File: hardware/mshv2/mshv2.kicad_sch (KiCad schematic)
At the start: 0 parts

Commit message: Finished part 1
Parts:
- added C1: 100uF/25V, symbol Device:C_Polarized
- added C2: 100uF/10V, symbol Device:C_Polarized
- added C3: 10uF, symbol Device:C
- added C4: 0.1uF, symbol Device:C
- added D1: MBRS340, Diode_SMD:D_SMC, symbol Diode:MBRS340
- added J1: 12V_INPUT, symbol Connector:Screw_Terminal_01x02
- added U1: LM2596S-3.3, Package_TO_SOT_SMD:TO-263-5_TabPin3, symbol Regulator_Switching:LM2596S-3.3
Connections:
- new net: C1.1, D1.1 (K), U1.1 (VIN), U1.5 (~{ON}/OFF)
- new net +12V: D1.2 (A), J1.1 (Pin_1)
- new net +3.3V: C2.1, C3.1, C4.1, U1.2 (OUT), U1.4 (FB)
- new net GND: C1.2, C2.2, C3.2, C4.2, J1.2 (Pin_2), U1.3 (GND)

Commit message: Part 2 WIP
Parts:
- added U2: ESP32-C6-WROOM-1-N8, PCM_Espressif:ESP32-C6-WROOM-1, symbol PCM_Espressif:ESP32-C6-WROOM-1
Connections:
- new net: U2.1 (GND), U2.28 (GND), U2.29 (GND)
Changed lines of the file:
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@@
+	)
+	(symbol
+		(lib_id "PCM_Espressif:ESP32-C6-WROOM-1")
+		(at 154.94 110.49 0)
+		(unit 1)
+		(exclude_from_sim no)
+		(in_bom yes)
+		(on_board yes)
+		(dnp no)
+		(fields_autoplaced yes)
+		(property "Reference" "U2"
+			(at 157.0833 74.93 0)
+			(effects
+				(font
+					(size 1.27 1.27)
+				)
+				(justify left)
+			)
+		)
+		(property "Value" "ESP32-C6-WROOM-1-N8"
+			(at 157.0833 77.47 0)
+			(effects
+				(font
+					(size 1.27 1.27)
+				)
+				(justify left)
+			)
+		)
+		(property "Footprint" "PCM_Espressif:ESP32-C6-WROOM-1"
+			(at 154.94 155.575 0)
+			(effects
+				(font
+					(size 1.27 1.27)
+				)
+				(hide yes)
+			)
+		)
+		(property "Datasheet" "https://www.espressif.com/sites/default/files/documentation/esp32-c6-wroom-1_wroom-1u_datasheet_en.pdf"
+			(at 154.94 158.75 0)
+			(effects
+				(font
+					(size 1.27 1.27)
+				)
+				(hide yes)
+			)
+		)
+		(property "Description" "ESP32-C6-WROOM-1/U is a module that supports 2.4 GHz Wi-Fi 6 (802.11 ax), Bluetooth® 5 (LE), Zigbee and Thread (802.15.4)"
+			(at 154.94 110.49 0)
+			(effects
+				(font
+					(size 1.27 1.27)
+				)
+				(hide yes)
+			)
+		)
+		(pin "4"
+		)
+		(pin "3"
+		)
+		(pin "26"
+		)
+		(pin "8"
+		)
+		(pin "9"
+		)
+		(pin "27"
+		)
+		(pin "6"
+		)
+		(pin "2"
+		)
+		(pin "1"
+		)
+		(pin "28"
+		)
+		(pin "29"
+		)
+		(pin "24"
+		)
+		(pin "22"
+		)
+		(pin "14"
+		)
+		(pin "5"
+		)
+		(pin "25"
+		)
+		(pin "7"
+		)
+		(pin "16"
+		)
+		(pin "17"
+		)
+		(pin "11"
+		)
+		(pin "20"
+		)
+		(pin "18"
+		)
+		(pin "10"
+		)
+		(pin "15"
+		)
+		(pin "19"
+		)
+		(pin "21"
+		)
+		(pin "12"
+		)
+		(pin "23"
+		)
+		(pin "13"
+		)
+		(instances
+			(project ""
+				(path "/71e681ae-2e40-4eed-9bbd-6e93cdfb5938"
+					(reference "U2")
+					(unit 1)
+				)
+			)
+		)
 	)
 	(symbol

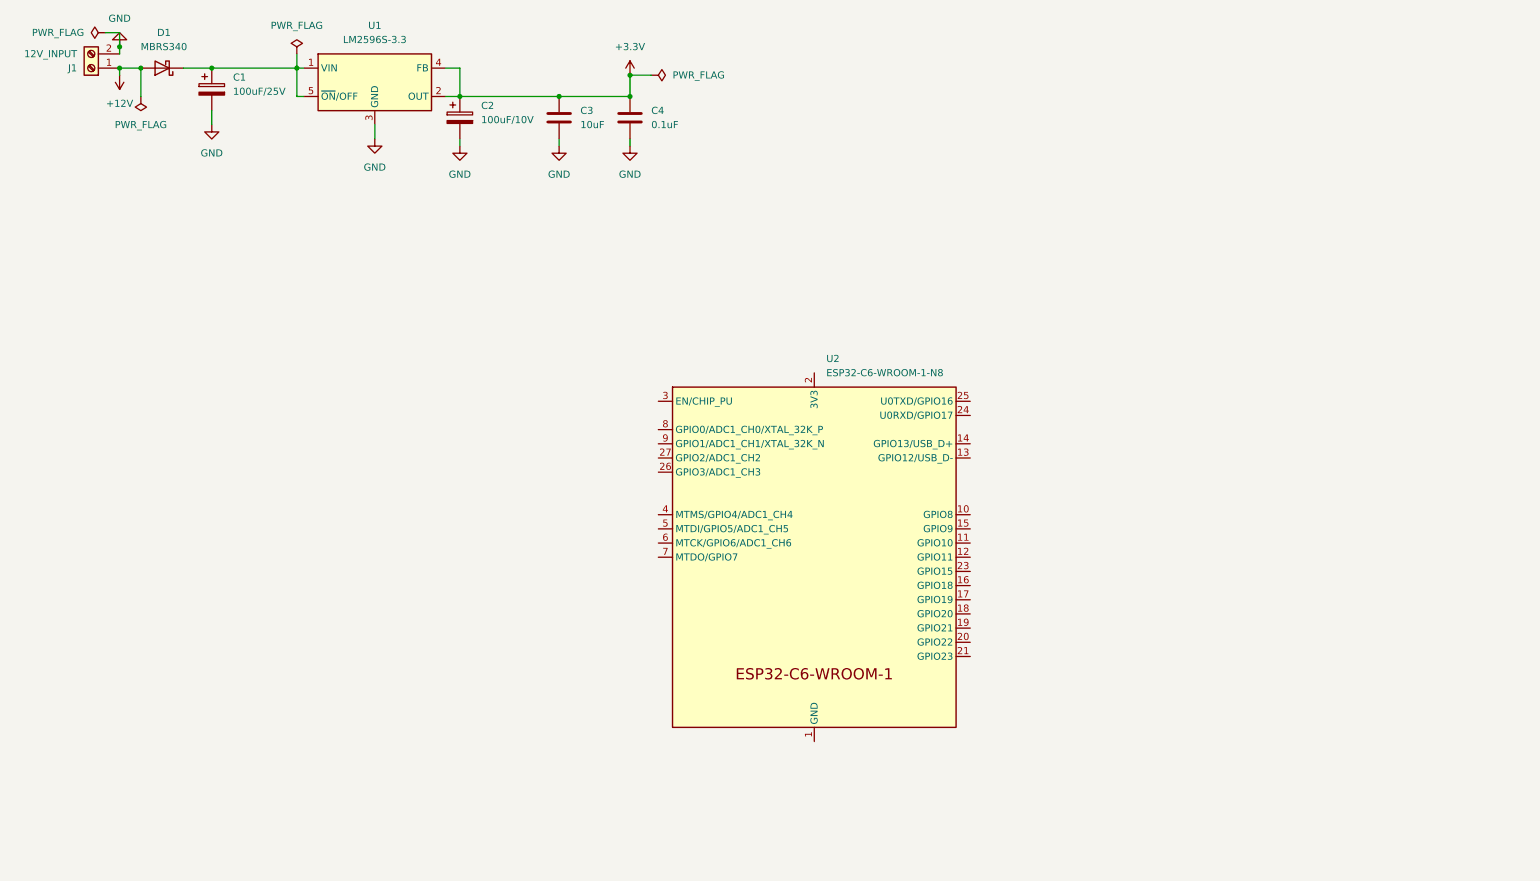
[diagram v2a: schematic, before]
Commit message: docs: Add comprehensive project documentation and dual power design
- Add complete README.md with project overview, features, and getting started guide
- Add BREADBOARD_PROTOTYPE.md with phased prototyping strategy and wiring diagrams
- Update KICAD_SCHEMATIC_GUIDE.md with dual power system (12V + USB-C)
  - Add AMS1117-3.3 LDO regulator for USB power path
  - Add B5819W Schottky OR-ing diodes (D_BUCK and D_USB)
  - Fix USB D+/D- GPIO pin assignments (GPIO12=D-, GPIO13=D+)
- Fix markdown linting issues across all documentation
  - Wrap long lines to 80 characters
  - Fix table formatting with proper spacing
  - Add blank lines around lists
- Update Hardware.md and Requirements.md for markdownlint compliance
- Update Claude.md with conventional commit specification reference
- Update hardware/mshv2/mshv2.kicad_sch with schematic progress

BREAKING CHANGE: Dual power design replaces simple USB connection approach

The new design allows automatic power source selection between 12V marine
power and USB-C, enabling both field deployment and bench testing without
hardware modifications.
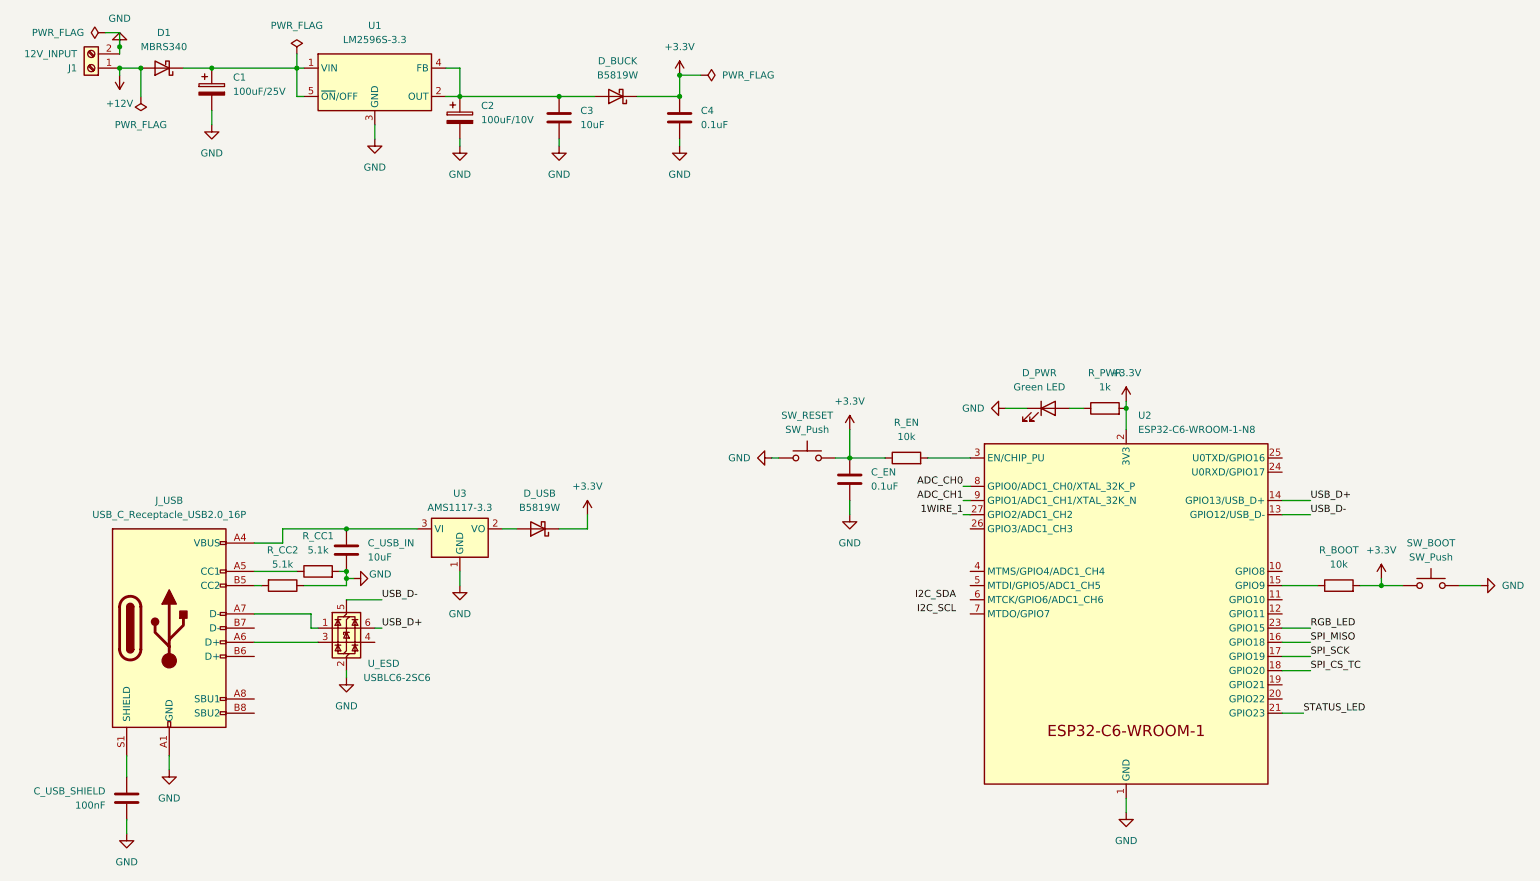
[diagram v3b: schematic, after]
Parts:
- added C_EN: 0.1uF, symbol Device:C
- added C_USB_IN: 10uF, symbol Device:C
- added C_USB_SHIELD: 100nF, symbol Device:C
- added D_BUCK, D_USB: B5819W, symbol Device:D_Schottky
- added D_PWR: Green LED, symbol Device:LED
- added J_USB: USB_C_Receptacle_USB2.0_16P, symbol Connector:USB_C_Receptacle_USB2.0_16P
- added R_BOOT, R_EN: 10k, symbol Device:R
- added R_CC1, R_CC2: 5.1k, symbol Device:R
- added R_PWR: 1k, symbol Device:R
- added SW_BOOT, SW_RESET: SW_Push, symbol Switch:SW_Push
- added U3: AMS1117-3.3, Package_TO_SOT_SMD:SOT-223-3_TabPin2, symbol Regulator_Linear:AMS1117-3.3
- added U_ESD: USBLC6-2SC6, Package_TO_SOT_SMD:SOT-23-6, symbol Power_Protection:USBLC6-2SC6
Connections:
- net +3.3V: now also U2.2 (3V3), C_EN.1, D_BUCK.1 (K), D_USB.1 (K), R_BOOT.2, R_EN.1, R_PWR.2, SW_BOOT.1, SW_RESET.2; no longer C2.1, C3.1, U1.2 (OUT), U1.4 (FB)
- net GND: now also U2.1 (GND), U2.28 (GND), U2.29 (GND), C_EN.2, C_USB_IN.2, C_USB_SHIELD.2, D_PWR.1 (K), J_USB.A1 (GND), J_USB.A12 (GND), J_USB.B1 (GND), J_USB.B12 (GND), R_CC1.2, R_CC2.1, SW_BOOT.2, SW_RESET.1, U3.1 (GND), U_ESD.2 (GND)
- net USB_D-: now reaches U2.13 (GPIO12/USB_D-)
- net USB_D-: now also U_ESD.5 (VBUS)
- net USB_D+: now reaches U2.14 (GPIO13/USB_D+)
- net USB_D+: now also U_ESD.6 (I/O1)
- net at U2.15 (GPIO9): now also R_BOOT.1
- net SPI_MISO: now reaches U2.16 (GPIO18)
- net SPI_SCK: now reaches U2.17 (GPIO19)
- net SPI_CS_TC: now reaches U2.18 (GPIO20)
- net STATUS_LED: now reaches U2.21 (GPIO23)
- net RGB_LED: now reaches U2.23 (GPIO15)
- net 1WIRE_1: now reaches U2.27 (GPIO2/ADC1_CH2)
- net at U2.3 (EN/CHIP_PU): now also R_EN.2
- net ADC_CH0: now reaches U2.8 (GPIO0/ADC1_CH0/XTAL_32K_P)
- net ADC_CH1: now reaches U2.9 (GPIO1/ADC1_CH1/XTAL_32K_N)
- new net: J_USB.A5 (CC1), R_CC1.1
- new net: C2.1, C3.1, D_BUCK.2 (A), U1.2 (OUT), U1.4 (FB)
- new net: C_USB_IN.1, J_USB.A4 (VBUS), J_USB.A9 (VBUS), J_USB.B4 (VBUS), J_USB.B9 (VBUS), U3.3 (VI)
- new net: D_PWR.2 (A), R_PWR.1
- new net: J_USB.A7 (D-), U_ESD.1 (I/O1)
- new net: J_USB.A6 (D+), U_ESD.3 (I/O2)
- new net: D_USB.2 (A), U3.2 (VO)
- new net: J_USB.B5 (CC2), R_CC2.2
- new net: C_USB_SHIELD.1, J_USB.S1 (SHIELD)
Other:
- moved on the sheet: C4, U2

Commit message: Updating claude directions and WIP on the schematic
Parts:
- added C_FILT_1, C_FILT_2, C_FILT_3, C_FILT_4, C_FILT_5, C_FILT_E_1, C_FILT_E_2, C_RGB1: 0.1uF, Capacitor_SMD:C_0201_0603Metric, symbol Device:C
- added D_RGB1: WS2812B, LED_SMD:LED_WS2812B_PLCC4_5.0x5.0mm_P3.2mm, symbol LED:WS2812B
- added D_STATUS1: Green LED, LED_SMD:LED_0603_1608Metric, symbol Device:LED
- added J2: CLAMP_1, TerminalBlock:TerminalBlock_MaiXu_MX126-5.0-02P_1x02_P5.00mm, symbol Connector:Screw_Terminal_01x02
- added J3: CLAMP_2, TerminalBlock:TerminalBlock_MaiXu_MX126-5.0-02P_1x02_P5.00mm, symbol Connector:Screw_Terminal_01x02
- added J4: CLAMP_3, TerminalBlock:TerminalBlock_MaiXu_MX126-5.0-02P_1x02_P5.00mm, symbol Connector:Screw_Terminal_01x02
- added J5: CLAMP_4, TerminalBlock:TerminalBlock_MaiXu_MX126-5.0-02P_1x02_P5.00mm, symbol Connector:Screw_Terminal_01x02
- added J6: CLAMP_5, TerminalBlock:TerminalBlock_MaiXu_MX126-5.0-02P_1x02_P5.00mm, symbol Connector:Screw_Terminal_01x02
- added R_DIV1_1, R_DIV1_2, R_DIV1_3, R_DIV1_4, R_DIV1_5: 10k, Resistor_SMD:R_0201_0603Metric, symbol Device:R
- added R_DIV2_1, R_DIV2_2, R_DIV2_3, R_DIV2_4, R_DIV2_5: 20k, Resistor_SMD:R_0201_0603Metric, symbol Device:R
- added R_FILT_1, R_FILT_2, R_FILT_3, R_FILT_4, R_FILT_5, R_SER_1, R_SER_2, R_SER_3, R_SER_4, R_SER_5: 1k, Resistor_SMD:R_0201_0603Metric, symbol Device:R
- added R_RBG1, R_STATUS1: 330, Resistor_SMD:R_0201_0603Metric, symbol Device:R
- added U2, U5: MCP6004, Package_SO:SOIC-14_3.9x8.7mm_P1.27mm, symbol Amplifier_Operational:MCP6004
- C1, C2, C3, C4: footprint (none) -> Capacitor_SMD:C_0201_0603Metric
- C_EN1: renamed from C_EN; footprint (none) -> Capacitor_SMD:C_0201_0603Metric
- C_USB_IN1: renamed from C_USB_IN; footprint (none) -> Capacitor_SMD:C_0201_0603Metric
- C_USB_SHIELD1: renamed from C_USB_SHIELD; footprint (none) -> Capacitor_SMD:C_0201_0603Metric
- D_BUCK1: renamed from D_BUCK; footprint (none) -> Diode_SMD:D_0201_0603Metric
- D_PWR1: renamed from D_PWR; footprint (none) -> LED_SMD:LED_0603_1608Metric
- D_USB1: renamed from D_USB; footprint (none) -> Diode_SMD:D_0201_0603Metric
- J1: footprint (none) -> TerminalBlock:TerminalBlock_MaiXu_MX126-5.0-02P_1x02_P5.00mm
- J_USB1: renamed from J_USB; footprint (none) -> Connector_USB:USB_C_Receptacle_GCT_USB4105-xx-A_16P_TopMnt_Horizontal
- R_BOOT1: renamed from R_BOOT; footprint (none) -> Resistor_SMD:R_0201_0603Metric
- R_CC1: renamed from R_CC2; footprint (none) -> Resistor_SMD:R_0201_0603Metric
- R_CC2: renamed from R_CC1; footprint (none) -> Resistor_SMD:R_0201_0603Metric
- R_EN1: renamed from R_EN; footprint (none) -> Resistor_SMD:R_0201_0603Metric
- R_PWR1: renamed from R_PWR; footprint (none) -> Resistor_SMD:R_0201_0603Metric
- SW_BOOT1: renamed from SW_BOOT; footprint (none) -> Button_Switch_THT:SW_Tactile_Straight_KSA0Axx1LFTR
- SW_RESET1: renamed from SW_RESET; footprint (none) -> Button_Switch_THT:SW_Tactile_Straight_KSA0Axx1LFTR
- renumbered U2 to U4, U_ESD to U_ESD1
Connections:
- net +3.3V: now also C_FILT_E_1.1, C_FILT_E_2.1, C_RGB1.2, D_RGB1.1 (VDD), U2.4 (V+), U5.4 (V+)
- net 1WIRE_1: now also U4.11 (GPIO10); no longer U4.27 (GPIO2/ADC1_CH2)
- net ADC_CH0: now also U2.1, U2.2 (-)
- net ADC_CH1: now also U2.6 (-), U2.7
- net GND: now also C_FILT_1.2, C_FILT_2.2, C_FILT_3.2, C_FILT_4.2, C_FILT_5.2, C_FILT_E_1.2, C_FILT_E_2.2, C_RGB1.1, D_RGB1.3 (VSS), D_STATUS1.1 (K), J2.2 (Pin_2), J3.2 (Pin_2), J4.2 (Pin_2), J5.2 (Pin_2), J6.2 (Pin_2), R_DIV2_1.2, R_DIV2_2.2, R_DIV2_3.2, R_DIV2_4.2, R_DIV2_5.2, U2.11 (V-), U5.11 (V-)
- net I2C_SCL: now also U4.7 (MTDO/GPIO7)
- net I2C_SDA: now also U4.6 (MTCK/GPIO6/ADC1_CH6)
- net RGB_LED: now also U4.10 (GPIO8), R_RBG1.1; no longer U4.23 (GPIO15)
- net STATUS_LED: now also R_STATUS1.1
- new net: J6.1 (Pin_1), R_SER_5.1
- new net: R_DIV1_5.2, R_SER_5.2
- new net: R_DIV1_3.1, R_DIV2_3.1, R_FILT_3.1
- new net: R_DIV1_4.1, R_DIV2_4.1, R_FILT_4.1
- new net: C_FILT_4.1, R_FILT_4.2, U2.12 (+)
- new net: J2.1 (Pin_1), R_SER_1.1
- new net: R_DIV1_1.2, R_SER_1.2
- new net: R_DIV1_5.1, R_DIV2_5.1, R_FILT_5.1
- new net: C_FILT_1.1, R_FILT_1.2, U2.3 (+)
- new net: R_DIV1_1.1, R_DIV2_1.1, R_FILT_1.1
- new net: C_FILT_2.1, R_FILT_2.2, U2.5 (+)
- new net: R_DIV1_3.2, R_SER_3.2
- new net: J5.1 (Pin_1), R_SER_4.1
- new net: R_DIV1_4.2, R_SER_4.2
- new net: J3.1 (Pin_1), R_SER_2.1
- new net: C_FILT_5.1, R_FILT_5.2, U5.12 (+)
- new net: R_DIV1_2.1, R_DIV2_2.1, R_FILT_2.1
- new net: R_DIV1_2.2, R_SER_2.2
- new net: C_FILT_3.1, R_FILT_3.2, U2.10 (+)
- new net: D_RGB1.4 (DIN), R_RBG1.2
- new net: D_STATUS1.2 (A), R_STATUS1.2
- new net: J4.1 (Pin_1), R_SER_3.1
- new net ADC_CH2: U2.8, U2.9 (-)
- new net ADC_CH3: U2.13 (-), U2.14
- new net ADC_CH4: U5.13 (-), U5.14
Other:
- title: ESP32-C6 Marine Sensor Board - Simplified -> ESP32 Marine Sensorhub v2
- moved on the sheet: C1, C2, C3, C4, C_EN1, C_USB_IN1, C_USB_SHIELD1, D1, D_BUCK1, D_PWR1, D_USB1, J1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

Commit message: Part 0 WIP
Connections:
- net +12V: no longer names the net of D1.2 (A), J1.1 (Pin_1)
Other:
- added sheet Current Sensing (sensors_current.kicad_sch)
- added sheet ESP32 (esp32.kicad_sch)
- added sheet Main Connector (connector_main.kicad_sch)
- added sheet Power Supply (power.kicad_sch)
- added sheet Temperature Sensors (sensors_temp.kicad_sch)
- added sheet Thermocouples (sensors_termocouple.kicad_sch)
- company: (none) -> Don McGarry
